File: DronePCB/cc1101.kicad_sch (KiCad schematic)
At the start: 12 parts, among them U2 CC1101RGPR, Y1 Crystal_GND24

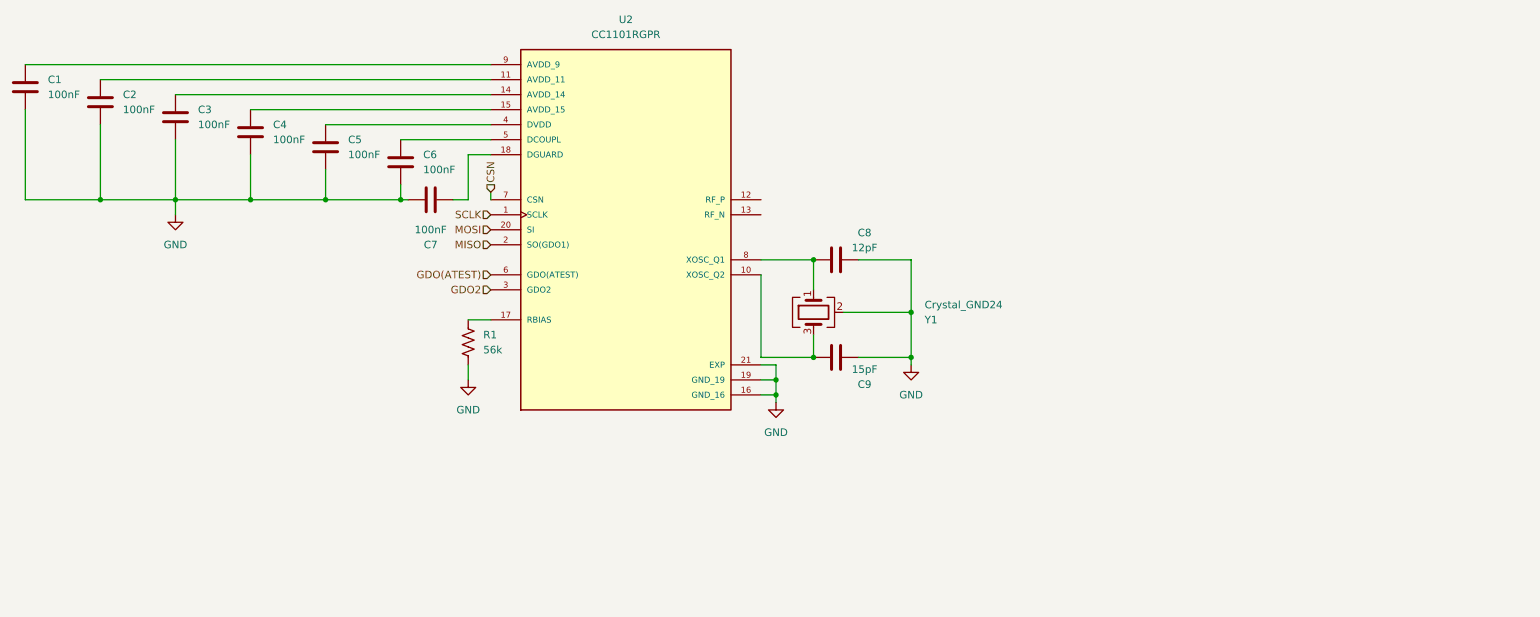
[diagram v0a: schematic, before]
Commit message: Completed CC1101 Radio Schematic
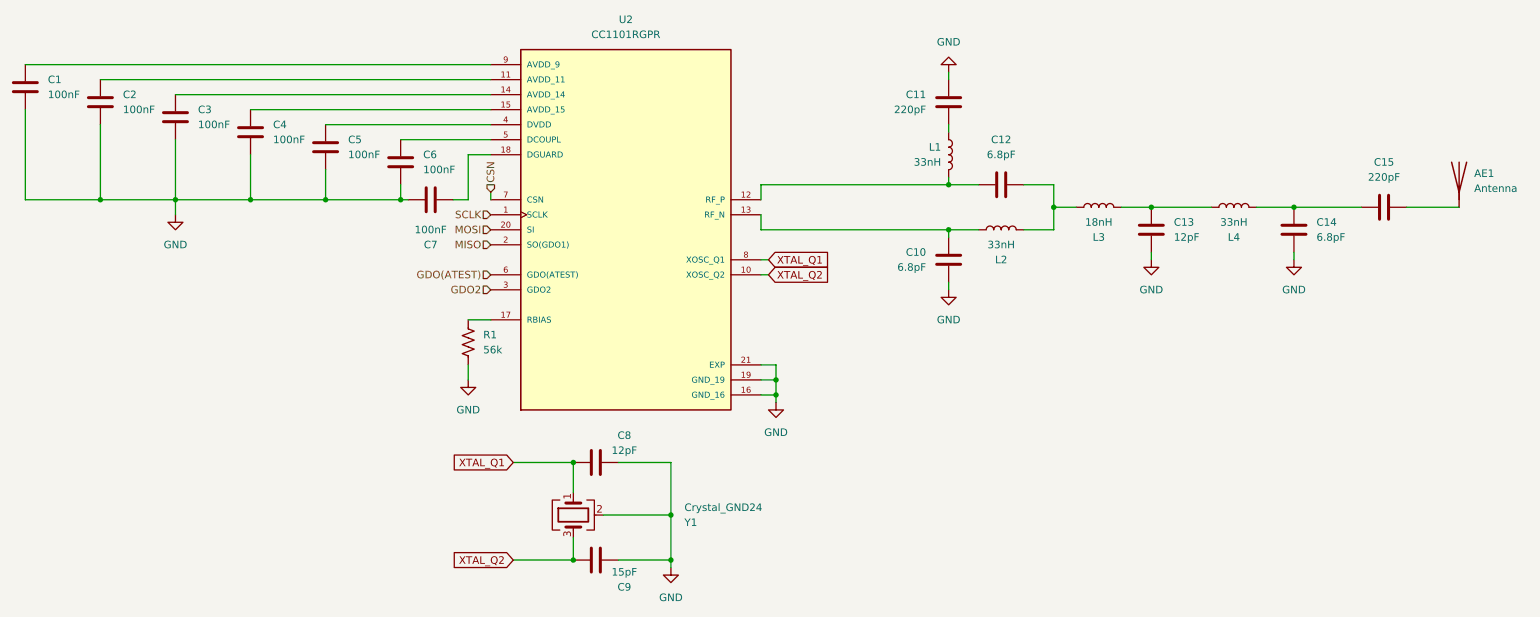
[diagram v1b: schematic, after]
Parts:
- added AE1: Antenna, symbol Device:Antenna
- added C10, C12, C14: 6.8pF, symbol Device:C
- added C11, C15: 220pF, symbol Device:C
- added C13: 12pF, symbol Device:C
- added L1, L2, L4: 33nH, symbol Device:L
- added L3: 18nH, symbol Device:L
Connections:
- net GND: now also C10.1, C11.2, C13.2, C14.2
- net XTAL_Q2: now reaches C9.1, U2.10 (XOSC_Q2), Y1.3
- net at U2.12 (RF_P): now also C12.2, L1.1
- net at U2.13 (RF_N): now also C10.2, L2.2
- net XTAL_Q1: now reaches C8.1, U2.8 (XOSC_Q1), Y1.1
- new net: C11.1, L1.2
- new net: C14.1, C15.1, L4.1
- new net: AE1.1 (A), C15.2
- new net: C12.1, L2.1, L3.2
- new net: C13.1, L3.1, L4.2
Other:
- moved on the sheet: C8, C9, Y1

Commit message: Finished and wired up CC1101 and Microphone circuits
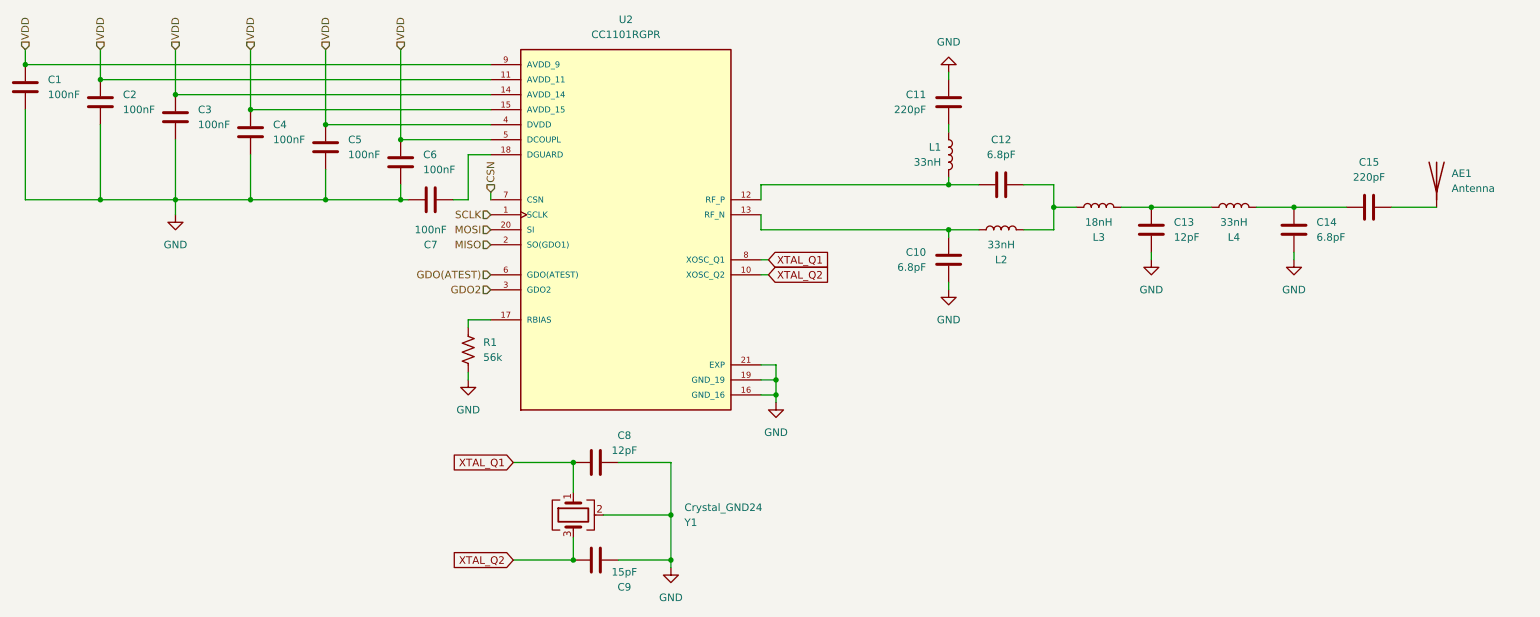
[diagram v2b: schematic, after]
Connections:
- net VDD: now reaches C2.1, U2.11 (AVDD_11)
- net VDD: now also C1.1, C3.1, C4.1, C5.1, C6.1, U2.14 (AVDD_14), U2.15 (AVDD_15), U2.4 (DVDD), U2.5 (DCOUPL), U2.9 (AVDD_9)
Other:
- moved on the sheet: AE1, C15, R1
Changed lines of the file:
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@@
+	)
+	(junction
+		(at 58.42 77.47)
+		(diameter 0)
+		(color 0 0 0 0)
 	)
 	(junction
@@
 	)
 	(junction
+		(at 20.32 69.85)
+		(diameter 0)
+		(color 0 0 0 0)
+	)
+	(junction
 		(at 45.72 92.71)
 		(diameter 0)
@@
 	)
 	(junction
+		(at 45.72 74.93)
+		(diameter 0)
+		(color 0 0 0 0)
+	)
+	(junction
 		(at 176.53 97.79)
 		(diameter 0)
@@
 	)
 	(junction
+		(at 83.82 82.55)
+		(diameter 0)
+		(color 0 0 0 0)
+	)
+	(junction
+		(at 33.02 72.39)
+		(diameter 0)
+		(color 0 0 0 0)
+	)
+	(junction
+		(at 71.12 80.01)
+		(diameter 0)
+		(color 0 0 0 0)
+	)
+	(junction
 		(at 147.32 123.19)
 		(diameter 0)
@@
 	(wire
 		(pts
+			(xy 20.32 67.31) (xy 20.32 69.85)
+		)
+		(stroke
+			(width 0)
+			(type default)
+		)
+	)
+	(wire
+		(pts
 			(xy 99.06 91.44) (xy 99.06 92.71)
 		)
@@
 	(wire
 		(pts
-			(xy 95.25 123.19) (xy 95.25 120.65)
+			(xy 95.25 123.19) (xy 95.25 121.92)
 		)
 		(stroke
@@
 	(wire
 		(pts
+			(xy 58.42 67.31) (xy 58.42 77.47)
+		)
+		(stroke
+			(width 0)
+			(type default)
+		)
+	)
+	(wire
+		(pts
+			(xy 45.72 67.31) (xy 45.72 74.93)
+		)
+		(stroke
+			(width 0)
+			(type default)
+		)
+	)
+	(wire
+		(pts
 			(xy 58.42 77.47) (xy 99.06 77.47)
 		)
@@
 	(wire
 		(pts
+			(xy 95.25 113.03) (xy 95.25 114.3)
+		)
+		(stroke
+			(width 0)
+			(type default)
+		)
+	)
+	(wire
+		(pts
 			(xy 205.74 93.98) (xy 210.82 93.98)
 		)
@@
 	(wire
 		(pts
-			(xy 234.95 93.98) (xy 246.38 93.98)
+			(xy 234.95 93.98) (xy 243.84 93.98)
 		)
 		(stroke
@@
 	(wire
 		(pts
+			(xy 45.72 74.93) (xy 99.06 74.93)
+		)
+		(stroke
+			(width 0)
+			(type default)
+		)
+	)
+	(wire
+		(pts
 			(xy 147.32 120.65) (xy 147.32 123.19)
 		)
@@
 	(wire
 		(pts
+			(xy 71.12 67.31) (xy 71.12 80.01)
+		)
+		(stroke
+			(width 0)
+			(type default)
+		)
+	)
+	(wire
+		(pts
 			(xy 33.02 92.71) (xy 45.72 92.71)
 		)
@@
 	(wire
 		(pts
+			(xy 33.02 67.31) (xy 33.02 72.39)
+		)
+		(stroke
+			(width 0)
+			(type default)
+		)
+	)
+	(wire
+		(pts
 			(xy 144.78 125.73) (xy 147.32 125.73)
 		)
@@
 	(wire
 		(pts
+			(xy 83.82 67.31) (xy 83.82 82.55)
+		)
+		(stroke
+			(width 0)
+			(type default)
+		)
+	)
+	(wire
+		(pts
 			(xy 146.05 102.87) (xy 144.78 102.87)
 		)
@@
 	(wire
 		(pts
-			(xy 262.89 93.98) (xy 254 93.98)
+			(xy 259.08 93.98) (xy 251.46 93.98)
 		)
 		(stroke
@@
 		(pts
 			(xy 194.31 97.79) (xy 189.23 97.79)
-		)
-		(stroke
-			(width 0)
-			(type default)
-		)
-	)
-	(wire
-		(pts
-			(xy 45.72 74.93) (xy 99.06 74.93)
 		)
 		(stroke
@@
 		)
 	)
+	(hierarchical_label "VDD"
+		(shape input)
+		(at 71.12 67.31 90)
+		(effects
+			(font
+				(size 1.27 1.27)
+			)
+			(justify left)
+		)
+	)
 	(hierarchical_label "GDO(ATEST)"
 		(shape input)
@@
 		)
 	)
+	(hierarchical_label "VDD"
+		(shape input)
+		(at 20.32 67.31 90)
+		(effects
+			(font
+				(size 1.27 1.27)
+			)
+			(justify left)
+		)
+	)
 	(hierarchical_label "MOSI"
 		(shape input)
@@
 		(shape input)
 		(at 99.06 91.44 90)
+		(effects
+			(font
+				(size 1.27 1.27)
+			)
+			(justify left)
+		)
+	)
+	(hierarchical_label "VDD"
+		(shape input)
+		(at 33.02 67.31 90)
+		(effects
+			(font
+				(size 1.27 1.27)
+			)
+			(justify left)
+		)
+	)
+	(hierarchical_label "VDD"
+		(shape input)
+		(at 83.82 67.31 90)
+		(effects
+			(font
+				(size 1.27 1.27)
+			)
+			(justify left)
+		)
+	)
+	(hierarchical_label "VDD"
+		(shape input)
+		(at 58.42 67.31 90)
+		(effects
+			(font
+				(size 1.27 1.27)
+			)
+			(justify left)
+		)
+	)
+	(hierarchical_label "VDD"
+		(shape input)
+		(at 45.72 67.31 90)
 		(effects
 			(font
@@
 	(symbol
 		(lib_id "Device:C")
-		(at 250.19 93.98 90)
+		(at 247.65 93.98 90)
 		(unit 1)
 		(exclude_from_sim no)
@@
 		(fields_autoplaced yes)
 		(property "Reference" "C15"
-			(at 250.19 86.36 90)
+			(at 247.65 86.36 90)
 			(effects
 				(font
@@
 		)
 		(property "Value" "220pF"
-			(at 250.19 88.9 90)
+			(at 247.65 88.9 90)
 			(effects
 				(font
@@
 		)
 		(property "Footprint" ""
-			(at 254 93.0148 0)
+			(at 251.46 93.0148 0)
 			(effects
 				(font
@@
 		)
 		(property "Datasheet" "~"
-			(at 250.19 93.98 0)
+			(at 247.65 93.98 0)
 			(effects
 				(font
@@
 		)
 		(property "Description" "Unpolarized capacitor"
-			(at 250.19 93.98 0)
+			(at 247.65 93.98 0)
 			(effects
 				(font
@@
 	(symbol
 		(lib_id "Device:Antenna")
-		(at 262.89 88.9 0)
+		(at 259.08 88.9 0)
 		(unit 1)
 		(exclude_from_sim no)
@@
 		(fields_autoplaced yes)
 		(property "Reference" "AE1"
-			(at 265.43 88.2649 0)
+			(at 261.62 88.2649 0)
 			(effects
 				(font
@@
 		)
 		(property "Value" "Antenna"
-			(at 265.43 90.8049 0)
+			(at 261.62 90.8049 0)
 			(effects
 				(font
@@
 		)
 		(property "Footprint" ""
-			(at 262.89 88.9 0)
+			(at 259.08 88.9 0)
 			(effects
 				(font
@@
 		)
 		(property "Datasheet" "~"
-			(at 262.89 88.9 0)
+			(at 259.08 88.9 0)
 			(effects
 				(font
@@
 		)
 		(property "Description" "Antenna"
-			(at 262.89 88.9 0)
+			(at 259.08 88.9 0)
 			(effects
 				(font
@@
 	(symbol
 		(lib_id "Device:R_US")
-		(at 95.25 116.84 0)
+		(at 95.25 118.11 0)
 		(unit 1)
 		(exclude_from_sim no)
@@
 		(fields_autoplaced yes)
 		(property "Reference" "R1"
-			(at 97.79 115.5699 0)
+			(at 97.79 116.8399 0)
 			(effects
 				(font
@@
 		)
 		(property "Value" "56k"
-			(at 97.79 118.1099 0)
+			(at 97.79 119.3799 0)
 			(effects
 				(font
@@
 		)
 		(property "Footprint" ""
-			(at 96.266 117.094 90)
+			(at 96.266 118.364 90)
 			(effects
 				(font
@@
 		)
 		(property "Datasheet" "~"
-			(at 95.25 116.84 0)
+			(at 95.25 118.11 0)
 			(effects
 				(font
@@
 		)
 		(property "Description" "Resistor, US symbol"
-			(at 95.25 116.84 0)
-			(effects
-				(font
+			(at 95.25 118.11 0)
+			(effects
+				(font

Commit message: Completed H-Bridge Circuit | Finished Schematic | Working on pcb design
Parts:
- AE1: footprint (none) -> ExternalParts:ANT1204F002R0315A
- C10: renamed from C11; footprint (none) -> Capacitor_SMD:C_0402_1005Metric
- C11: renamed from C10; footprint (none) -> Capacitor_SMD:C_0402_1005Metric
- C12, C13, C14, C15: footprint (none) -> Capacitor_SMD:C_0402_1005Metric
- L1, L2, L3, L4: footprint (none) -> Inductor_SMD:L_0402_1005Metric
- R3: renamed from R1; footprint (none) -> Resistor_SMD:R_0603_1608Metric
- U2: footprint CC1101RGPR:QFN50P400X400X100-21N -> ExternalParts:QFN50P400X400X100-21N
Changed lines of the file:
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@@
 			)
 		)
-		(property "Footprint" "CC1101RGPR:QFN50P400X400X100-21N"
+		(property "Footprint" "ExternalParts:QFN50P400X400X100-21N"
 			(at 121.92 97.79 0)
 			(hide yes)
@@
 		(in_pos_files yes)
 		(dnp no)
-		(property "Reference" "C11"
+		(property "Reference" "C10"
 			(at 172.72 74.9299 0)
 			(show_name no)
@@
 			)
 		)
-		(property "Footprint" ""
+		(property "Footprint" "Capacitor_SMD:C_0402_1005Metric"
 			(at 177.4952 72.39 0)
 			(hide yes)
@@
 			(project "DronePCB"
 				(path "/c9b74494-ac48-4f27-9459-39f0e04d9d05/b72735a3-baa6-4eaf-854a-296625361d8a"
-					(reference "C11")
+					(reference "C10")
 					(unit 1)
 				)
@@
 			)
 		)
-		(property "Footprint" ""
+		(property "Footprint" "Capacitor_SMD:C_0402_1005Metric"
 			(at 235.9152 101.6 0)
 			(hide yes)
@@
 			)
 		)
-		(property "Footprint" ""
+		(property "Footprint" "Capacitor_SMD:C_0402_1005Metric"
 			(at 251.46 93.0148 0)
 			(hide yes)
@@
 		(in_pos_files yes)
 		(dnp no)
-		(property "Reference" "#PWR05"
+		(property "Reference" "#PWR019"
 			(at 176.53 114.3 0)
 			(hide yes)
@@
 			(project "DronePCB"
 				(path "/c9b74494-ac48-4f27-9459-39f0e04d9d05/b72735a3-baa6-4eaf-854a-296625361d8a"
-					(reference "#PWR05")
+					(reference "#PWR019")
 					(unit 1)
 				)
@@
 		(dnp no)
 		(fields_autoplaced yes)
-		(property "Reference" "#PWR04"
+		(property "Reference" "#PWR016"
 			(at 129.54 161.29 0)
 			(hide yes)
@@
 			(project "DronePCB"
 				(path "/c9b74494-ac48-4f27-9459-39f0e04d9d05/b72735a3-baa6-4eaf-854a-296625361d8a"
-					(reference "#PWR04")
+					(reference "#PWR016")
 					(unit 1)
 				)
@@
 		(dnp no)
 		(fields_autoplaced yes)
-		(property "Reference" "#PWR01"
+		(property "Reference" "#PWR015"
 			(at 95.25 129.54 0)
 			(hide yes)
@@
 			(project "DronePCB"
 				(path "/c9b74494-ac48-4f27-9459-39f0e04d9d05/b72735a3-baa6-4eaf-854a-296625361d8a"
-					(reference "#PWR01")
+					(reference "#PWR015")
 					(unit 1)
 				)
@@
 			)
 		)
-		(property "Footprint" ""
+		(property "Footprint" "Inductor_SMD:L_0402_1005Metric"
 			(at 176.53 85.09 0)
 			(hide yes)
@@
 			)
 		)
-		(property "Footprint" ""
+		(property "Footprint" "Inductor_SMD:L_0402_1005Metric"
 			(at 185.42 97.79 0)
 			(hide yes)
@@
 			)
 		)
-		(property "Footprint" ""
+		(property "Footprint" "Capacitor_SMD:C_0402_1005Metric"
 			(at 211.7852 101.6 0)
 			(hide yes)
@@
 		(in_pos_files yes)
 		(dnp no)
-		(property "Reference" "#PWR07"
+		(property "Reference" "#PWR020"
 			(at 210.82 109.22 0)
 			(hide yes)
@@
 			(project "DronePCB"
 				(path "/c9b74494-ac48-4f27-9459-39f0e04d9d05/b72735a3-baa6-4eaf-854a-296625361d8a"
-					(reference "#PWR07")
+					(reference "#PWR020")
 					(unit 1)
 				)
@@
 			)
 		)
-		(property "Footprint" ""
+		(property "Footprint" "ExternalParts:ANT1204F002R0315A"
 			(at 259.08 88.9 0)
 			(hide yes)
@@
 			)
 		)
-		(property "Footprint" ""
+		(property "Footprint" "Inductor_SMD:L_0402_1005Metric"
 			(at 224.79 93.98 0)
 			(hide yes)
@@
 		(dnp no)
 		(fields_autoplaced yes)
-		(property "Reference" "R1"
+		(property "Reference" "R3"
 			(at 97.79 116.8399 0)
 			(show_name no)
@@
 			)
 		)
-		(property "Footprint" ""
+		(property "Footprint" "Resistor_SMD:R_0603_1608Metric"
 			(at 96.266 118.364 90)
 			(hide yes)
@@
 			(project "DronePCB"
 				(path "/c9b74494-ac48-4f27-9459-39f0e04d9d05/b72735a3-baa6-4eaf-854a-296625361d8a"
-					(reference "R1")
+					(reference "R3")
 					(unit 1)
 				)
@@
 		(in_pos_files yes)
 		(dnp no)
-		(property "Reference" "#PWR06"
+		(property "Reference" "#PWR018"
 			(at 176.53 64.77 0)
 			(hide yes)
@@
 			(project "DronePCB"
 				(path "/c9b74494-ac48-4f27-9459-39f0e04d9d05/b72735a3-baa6-4eaf-854a-296625361d8a"
-					(reference "#PWR06")
+					(reference "#PWR018")
 					(unit 1)
 				)
@@
 			)
 		)
-		(property "Footprint" ""
+		(property "Footprint" "Inductor_SMD:L_0402_1005Metric"
 			(at 201.93 93.98 0)
 			(hide yes)
@@
 			)
 		)
-		(property "Footprint" ""
+		(property "Footprint" "Capacitor_SMD:C_0402_1005Metric"
 			(at 181.61 91.1352 0)
 			(hide yes)
@@
 		(dnp no)
 		(fields_autoplaced yes)
-		(property "Reference" "#PWR03"
+		(property "Reference" "#PWR017"
 			(at 147.32 133.35 0)
 			(hide yes)
@@
 			(project "DronePCB"
 				(path "/c9b74494-ac48-4f27-9459-39f0e04d9d05/b72735a3-baa6-4eaf-854a-296625361d8a"
-					(reference "#PWR03")
+					(reference "#PWR017")
 					(unit 1)
 				)
@@
 		(in_pos_files yes)
 		(dnp no)
-		(property "Reference" "C10"
+		(property "Reference" "C11"
 			(at 172.72 101.5999 0)
 			(show_name no)
@@
 			)
 		)
-		(property "Footprint" ""
+		(property "Footprint" "Capacitor_SMD:C_0402_1005Metric"
 			(at 177.4952 99.06 0)
 			(hide yes)
@@
 			(project "DronePCB"
 				(path "/c9b74494-ac48-4f27-9459-39f0e04d9d05/b72735a3-baa6-4eaf-854a-296625361d8a"
-					(reference "C10")
+					(reference "C11")
 					(unit 1)
 				)
@@
 		(in_pos_files yes)
 		(dnp no)
-		(property "Reference" "#PWR08"
+		(property "Reference" "#PWR021"
 			(at 234.95 109.22 0)
 			(hide yes)
@@
 			(project "DronePCB"
 				(path "/c9b74494-ac48-4f27-9459-39f0e04d9d05/b72735a3-baa6-4eaf-854a-296625361d8a"
-					(reference "#PWR08")
+					(reference "#PWR021")
 					(unit 1)
 				)
@@
 		(dnp no)
 		(fields_autoplaced yes)
-		(property "Reference" "#PWR02"
+		(property "Reference" "#PWR014"
 			(at 45.72 101.6 0)
 			(hide yes)
@@
 			(project "DronePCB"
 				(path "/c9b74494-ac48-4f27-9459-39f0e04d9d05/b72735a3-baa6-4eaf-854a-296625361d8a"
-					(reference "#PWR02")
-					(unit 1)
-				)
+					(reference "#PWR014")
+					(unit 1)
+				)

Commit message: Finished CC1101 Radio Circuit
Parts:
- Y1: value Crystal_GND24 -> NX3225GA; footprint Crystal:Crystal_SMD_0603-4Pin_6.0x3.5mm -> Crystal:Crystal_SMD_3225-4Pin_3.2x2.5mm
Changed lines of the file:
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@@
 			)
 		)
-		(property "Value" "Crystal_GND24"
+		(property "Value" "NX3225GA"
 			(at 131.826 144.78 90)
 			(show_name no)
@@
 			)
 		)
-		(property "Footprint" "Crystal:Crystal_SMD_0603-4Pin_6.0x3.5mm"
+		(property "Footprint" "Crystal:Crystal_SMD_3225-4Pin_3.2x2.5mm"
 			(at 113.03 146.05 0)
 			(hide yes)
